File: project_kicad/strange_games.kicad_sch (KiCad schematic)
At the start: 122 parts, among them J1 Display, M1 Motor_DC, Q1 Si2302A, Q2 Q_Photo, Q3 Si2302A, Q4 Q_Photo, SW1 SW_Push, SW10 SW_Push, SW2 SW_Push, SW3 SW_Push, SW4 SW_Push, SW5 SW_Push, SW6 SW_Push, SW7 SW_Push, SW8 SW_Push, SW9 SW_Push, U1 charge controller, U2 boost converter, U3 LDL1117S33R, U4 ESP32-DEVKIT-V1, U5 TMP112xxDRL, U6 vibrating_sensor, U7 LSM6DS3, U8 MQ-135 gas sensor

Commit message: pcb changes
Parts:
- added R34, R35, R36, R37, R38, R39, R40, R41: 10k_0805, PCM_4ms_Resistor:R_0805_2012Metric, symbol Library:1.2k_0603
- R10, R13, R14, R15, R21, R22, R23, R28, R29, R3, R30, R8: value 10k_0805 -> 100_0805; Display 10k -> 100; Specifications 10K, 1%, 1/10W, 0805 -> 100, 1%, 1/10W, 0805
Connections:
- net B1: now also R13.2; no longer R13.1
- net B10: now also R3.2; no longer R3.1
- net B2: now also R14.2; no longer R14.1
- net B3: now also R28.2; no longer R15.1
- net B4: now also R15.2; no longer R21.1
- net B5: now also R23.2; no longer R22.1
- net B6: now also R29.2; no longer R23.1
- net B7: now also R21.2; no longer R28.1
- net B8: now also R22.2; no longer R29.1
- net B9: now also R30.2; no longer R30.1
- net GND: now also R34.2, R35.2, R36.2, R37.2, R38.2, R39.2, R40.2, R41.2
- net at R18.2, SW3.2: now also R14.1; no longer R14.2
- net at R25.2, SW6.2: now also R23.1; no longer R22.2
- net at R24.2, SW5.2: now also R15.1; no longer R21.2
- net at R31.2, SW8.2: now also R21.1; no longer R28.2
- net at R17.2, SW2.2: now also R13.1; no longer R13.2
- net at R4.2, SW1.2: now also R3.1; no longer R3.2
- net at R32.2, SW9.2: now also R22.1; no longer R29.2
- net at R33.2, SW10.2: now also R30.1; no longer R30.2
- net at U7.2 (SDX): now also R40.1
- net at U7.3 (SCX): now also R41.1
- net at R26.2, SW7.2: now also R29.1; no longer R23.2
- net at R19.2, SW4.2: now also R28.1; no longer R15.2
- net at J1.24 (D5): now also R34.1
- net at J1.25 (D4): now also R35.1
- net at J1.26 (D3): now also R39.1
- net at J1.27 (D2): now also R38.1
- net at J1.28 (D1): now also R37.1
- net at J1.29 (D0): now also R36.1
- no-connect marks 15 -> 7
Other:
- moved on the sheet: Q2, Q4, R12, R16

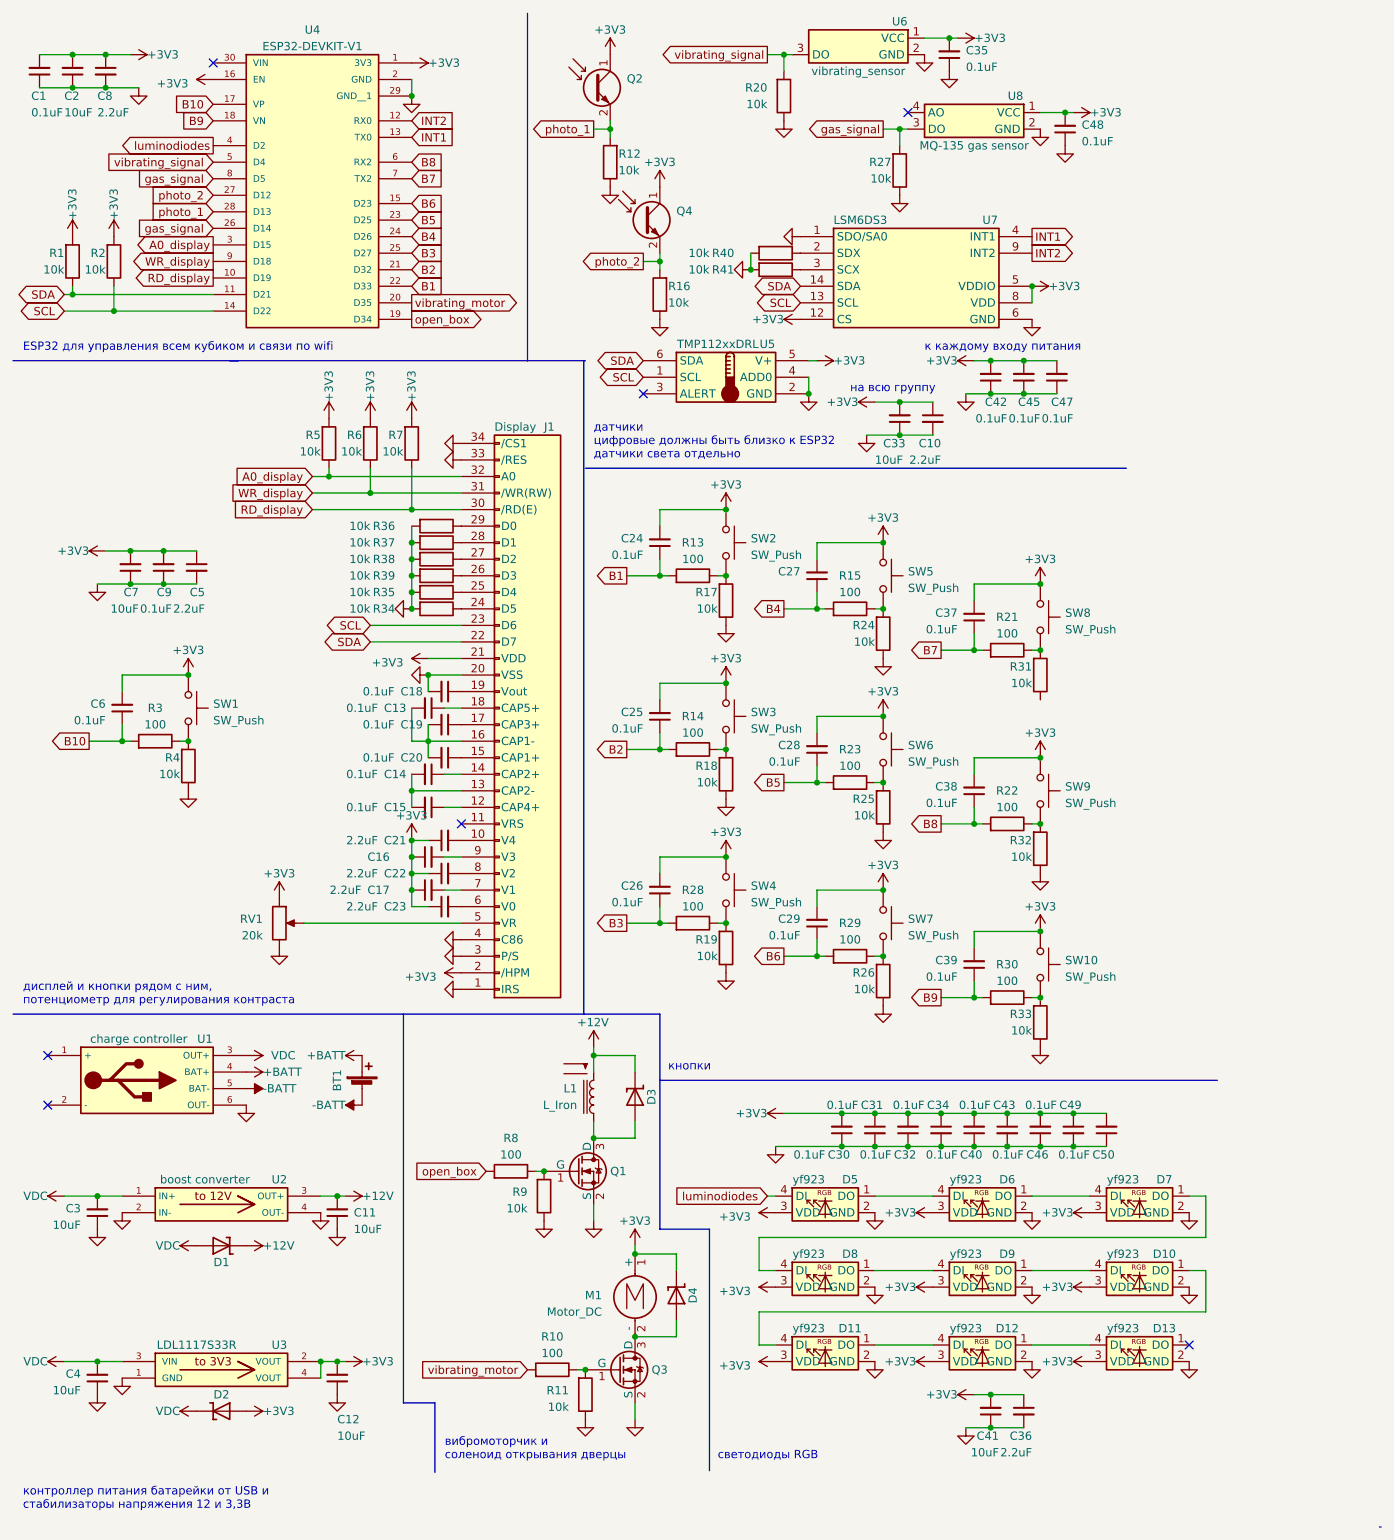
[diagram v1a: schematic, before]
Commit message: changed 10kR to 330R
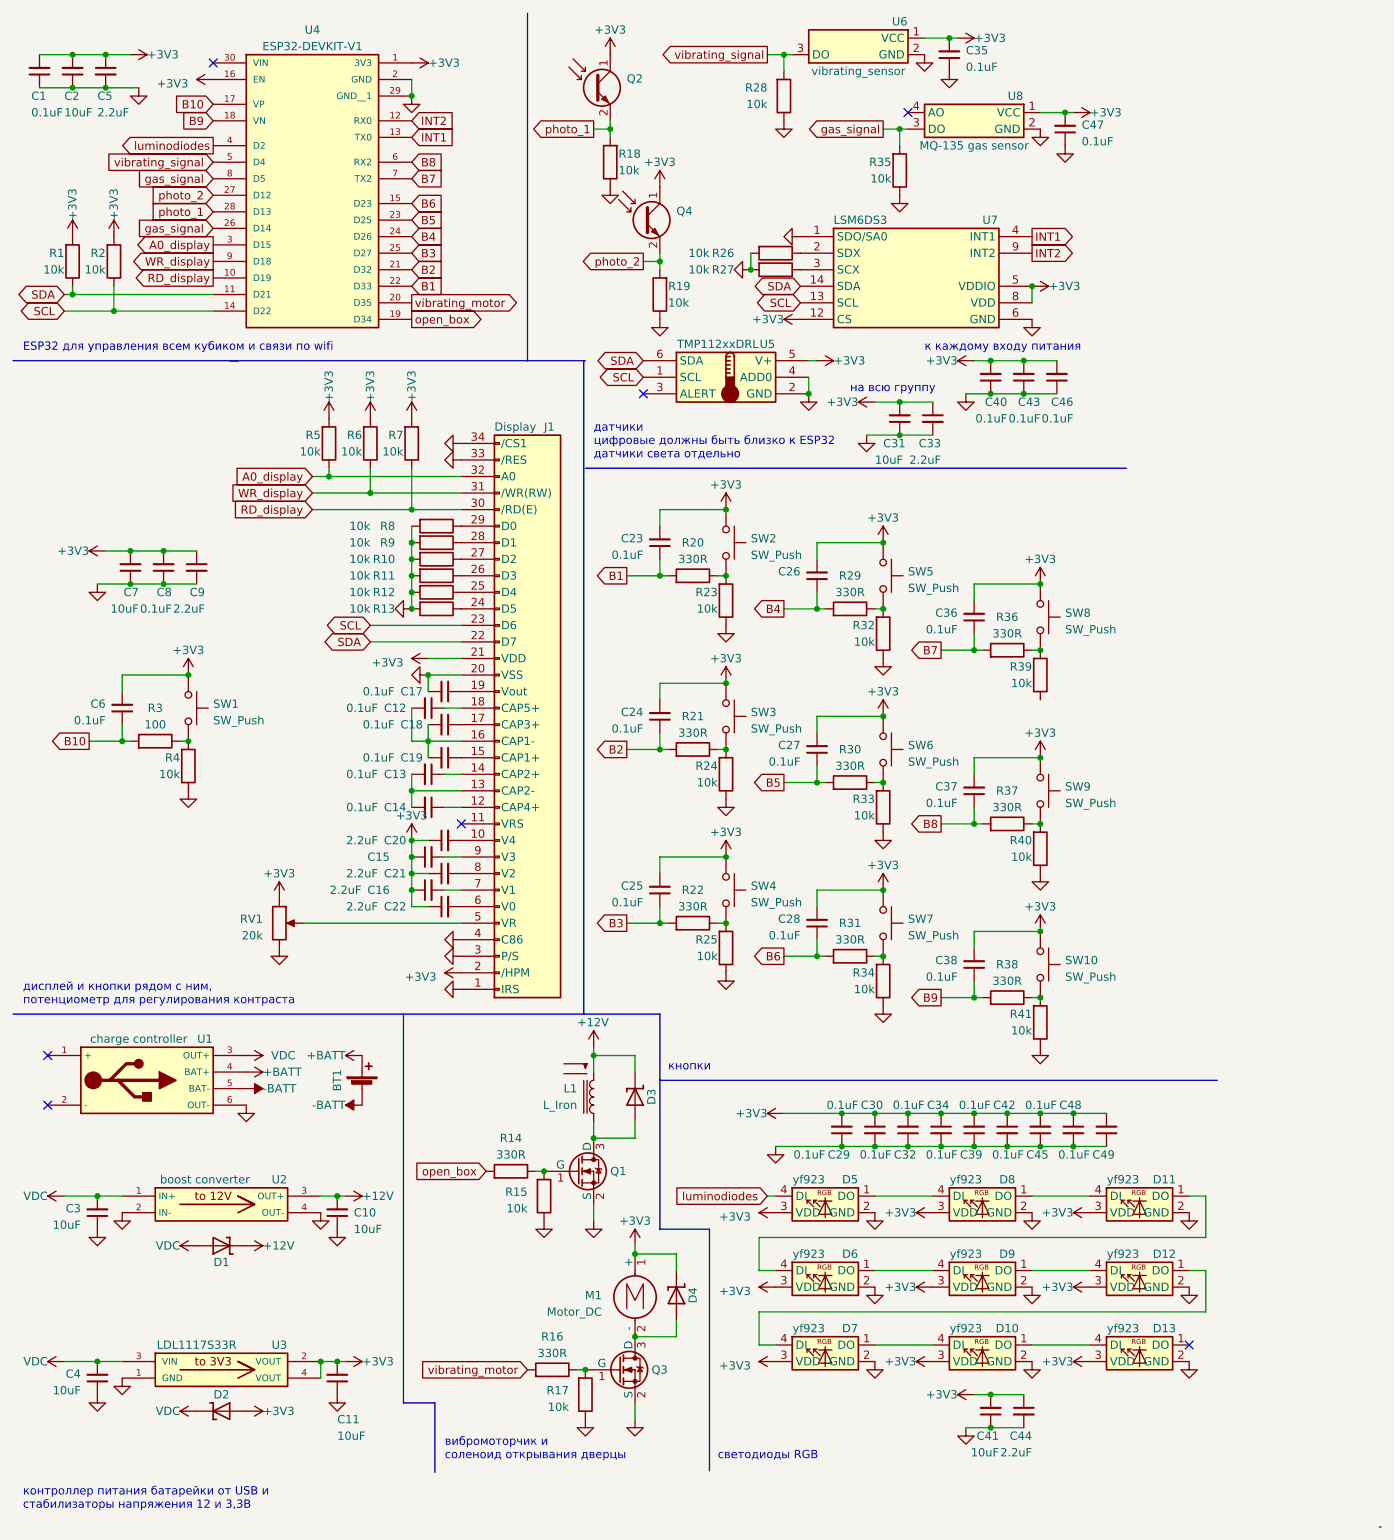
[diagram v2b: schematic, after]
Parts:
- removed R10, R13, R15, R21, R23, R28, R8: 100_0805, PCM_4ms_Resistor:R_0805_2012Metric, symbol Library:1.2k_0603
- added R14, R16, R20, R31, R36, R37, R38: 330_0805, PCM_4ms_Resistor:R_0805_2012Metric, symbol Library:1.2k_0603
- R21: renamed from R14; value 100_0805 -> 330_0805; Display 100 -> 330R; Specifications 100, 1%, 1/10W, 0805 -> 330, 1%, 1/10W, 0805
- R22, R29, R30: value 100_0805 -> 330_0805; Display 100 -> 330R; Specifications 100, 1%, 1/10W, 0805 -> 330, 1%, 1/10W, 0805
- renumbered C11 to C10, C12 to C11, C13 to C12, C14 to C13, C15 to C14, C16 to C15, C17 to C16, C18 to C17, C19 to C18, C20 to C19, C21 to C20, C22 to C21, C23 to C22, C24 to C23, C25 to C24, C26 to C25, C27 to C26, C28 to C27, C29 to C28, C30 to C29, C31 to C30, C33 to C31, C10 to C33, C37 to C36, C38 to C37, C39 to C38, C40 to C39, C42 to C40, C43 to C42, C45 to C43, C36 to C44, C46 to C45, C47 to C46, C48 to C47, C49 to C48, C50 to C49, C8 to C5, C9 to C8, C5 to C9, D12 to D10, D7 to D11, D10 to D12, D8 to D6, D11 to D7, D6 to D8, R38 to R10, R39 to R11, R35 to R12, R34 to R13, R9 to R15, R11 to R17, R12 to R18, R16 to R19, R17 to R23, R18 to R24, R19 to R25, R40 to R26, R41 to R27, R20 to R28, R24 to R32, R25 to R33, R26 to R34, R27 to R35, R31 to R39, R32 to R40, R33 to R41, R36 to R8, R37 to R9
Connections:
- net B1: now also R20.2
- net B3: now also R22.2
- net B4: now also R29.2
- net B5: now also R30.2
- net B6: now also R31.2; no longer R29.2
- net B7: now also R36.2
- net B8: now also R37.2; no longer R22.2
- net B9: now also R38.2; no longer R30.2
- net open_box: now also R14.2
- net vibrating_motor: now also R16.2
- net at R33.2, SW6.2: now also R30.1
- net at R39.2, SW8.2: now also R36.1
- net at R23.2, SW2.2: now also R20.1
- net at R40.2, SW9.2: now also R37.1; no longer R22.1
- net at R41.2, SW10.2: now also R38.1; no longer R30.1
- net at Q1.1 (G), R15.2: now also R14.1
- net at R32.2, SW5.2: now also R29.1
- net at R34.2, SW7.2: now also R31.1; no longer R29.1
- net at Q3.1 (G), R17.2: now also R16.1
- net at R25.2, SW4.2: now also R22.1

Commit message: pcb changes
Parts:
- U8: footprint Connector_PinHeader_1.27mm:PinHeader_1x04_P1.27mm_Vertical -> Connector_PinHeader_2.54mm:PinHeader_1x04_P2.54mm_Vertical
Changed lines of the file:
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@@
       (effects (font (size 1.27 1.27)))
     )
-    (property "Footprint" "Connector_PinHeader_1.27mm:PinHeader_1x04_P1.27mm_Vertical" (at 165.1 15.24 0)
+    (property "Footprint" "Connector_PinHeader_2.54mm:PinHeader_1x04_P2.54mm_Vertical" (at 165.1 15.24 0)
       (effects (font (size 1.27 1.27)) hide)
     )
